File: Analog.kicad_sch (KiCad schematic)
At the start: 42 parts, among them IC1 AMC1350DWVR, IC2 AMC1350DWVR, IC3 ZXRE160AET5TA, U2 TLV9001IDBVR, U3 TLV9001IDBVR

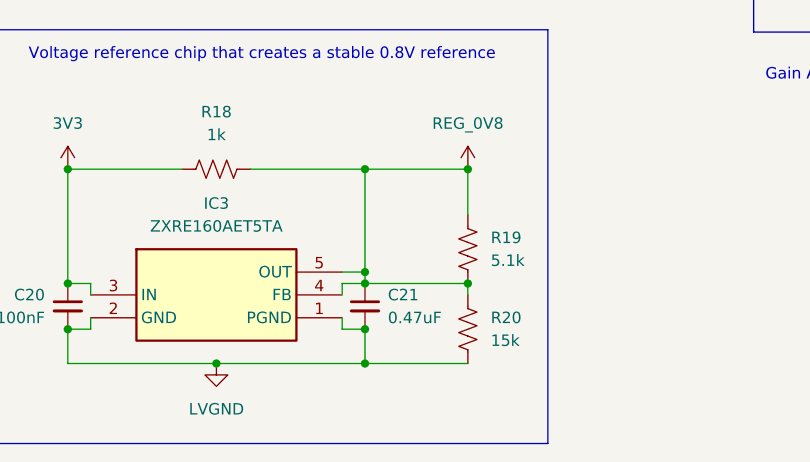
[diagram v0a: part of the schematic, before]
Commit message: Fixed 0.8V reference circuit short on accidental node for divider side
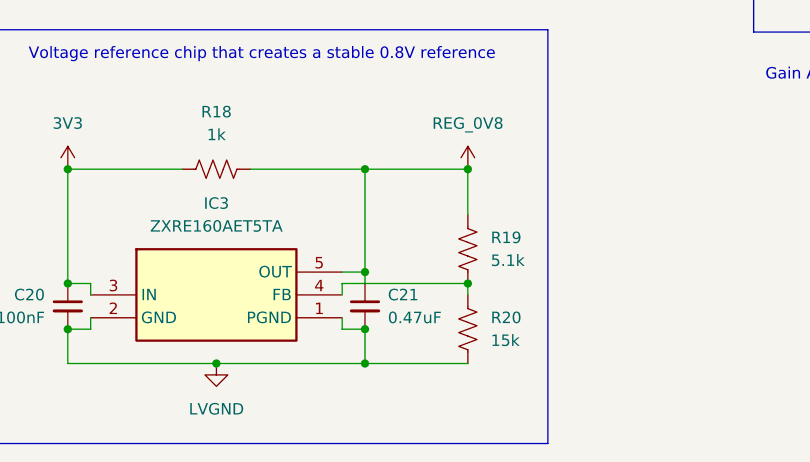
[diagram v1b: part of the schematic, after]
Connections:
- net REG_0V8: no longer IC3.4 (FB), R19.1, R20.1
- new net: IC3.4 (FB), R19.1, R20.1
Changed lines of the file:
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@@
-	)
-	(junction
-		(at 144.78 144.78)
-		(diameter 0)
-		(color 0 0 0 0)
 	)
 	(junction
@@
 	)
 	(junction
+		(at 66.04 53.34)
+		(diameter 0)
+		(color 0 0 0 0)
+	)
+	(junction
+		(at 218.44 54.61)
+		(diameter 0)
+		(color 0 0 0 0)
+	)
+	(junction
+		(at 36.83 53.34)
+		(diameter 0)
+		(color 0 0 0 0)
+	)
+	(junction
+		(at 229.87 67.31)
+		(diameter 0)
+		(color 0 0 0 0)
+	)
+	(junction
+		(at 157.48 59.69)
+		(diameter 0)
+		(color 0 0 0 0)
+	)
+	(junction
+		(at 128.27 153.67)
+		(diameter 0)
+		(color 0 0 0 0)
+	)
+	(junction
+		(at 116.84 46.99)
+		(diameter 0)
+		(color 0 0 0 0)
+	)
+	(junction
+		(at 77.47 53.34)
+		(diameter 0)
+		(color 0 0 0 0)
+	)
+	(junction
+		(at 144.78 132.08)
+		(diameter 0)
+		(color 0 0 0 0)
+	)
+	(junction
+		(at 156.21 132.08)
+		(diameter 0)
+		(color 0 0 0 0)
+	)
+	(junction
+		(at 116.84 82.55)
+		(diameter 0)
+		(color 0 0 0 0)
+	)
+	(junction
+		(at 124.46 54.61)
+		(diameter 0)
+		(color 0 0 0 0)
+	)
+	(junction
+		(at 157.48 90.17)
+		(diameter 0)
+		(color 0 0 0 0)
+	)
+	(junction
+		(at 116.84 87.63)
+		(diameter 0)
+		(color 0 0 0 0)
+	)
+	(junction
 		(at 156.21 144.78)
 		(diameter 0)
@@
 	)
 	(junction
-		(at 66.04 53.34)
-		(diameter 0)
-		(color 0 0 0 0)
-	)
-	(junction
-		(at 218.44 54.61)
-		(diameter 0)
-		(color 0 0 0 0)
-	)
-	(junction
-		(at 36.83 53.34)
-		(diameter 0)
-		(color 0 0 0 0)
-	)
-	(junction
-		(at 229.87 67.31)
-		(diameter 0)
-		(color 0 0 0 0)
-	)
-	(junction
-		(at 157.48 59.69)
-		(diameter 0)
-		(color 0 0 0 0)
-	)
-	(junction
-		(at 128.27 153.67)
-		(diameter 0)
-		(color 0 0 0 0)
-	)
-	(junction
-		(at 116.84 46.99)
-		(diameter 0)
-		(color 0 0 0 0)
-	)
-	(junction
-		(at 77.47 53.34)
-		(diameter 0)
-		(color 0 0 0 0)
-	)
-	(junction
-		(at 144.78 132.08)
-		(diameter 0)
-		(color 0 0 0 0)
-	)
-	(junction
-		(at 156.21 132.08)
-		(diameter 0)
-		(color 0 0 0 0)
-	)
-	(junction
-		(at 116.84 82.55)
-		(diameter 0)
-		(color 0 0 0 0)
-	)
-	(junction
-		(at 124.46 54.61)
-		(diameter 0)
-		(color 0 0 0 0)
-	)
-	(junction
-		(at 157.48 90.17)
-		(diameter 0)
-		(color 0 0 0 0)
-	)
-	(junction
-		(at 116.84 87.63)
-		(diameter 0)
-		(color 0 0 0 0)
-	)
-	(junction
 		(at 111.76 144.78)
 		(diameter 0)
@@
 	(wire
 		(pts
-			(xy 142.24 144.78) (xy 144.78 144.78)
-		)
-		(stroke
-			(width 0)
-			(type default)
-		)
-	)
-	(wire
-		(pts
 			(xy 124.46 81.28) (xy 127 81.28)
 		)
@@
 	(wire
 		(pts
-			(xy 144.78 144.78) (xy 156.21 144.78)
-		)
-		(stroke
-			(width 0)
-			(type default)
-		)
-	)
-	(wire
-		(pts
 			(xy 144.78 132.08) (xy 156.21 132.08)
 		)
@@
 		)
 		(stroke
+			(width 0)
+			(type default)
+		)
+	)
+	(wire
+		(pts
+			(xy 142.24 144.78) (xy 156.21 144.78)
+		)
+		(stroke

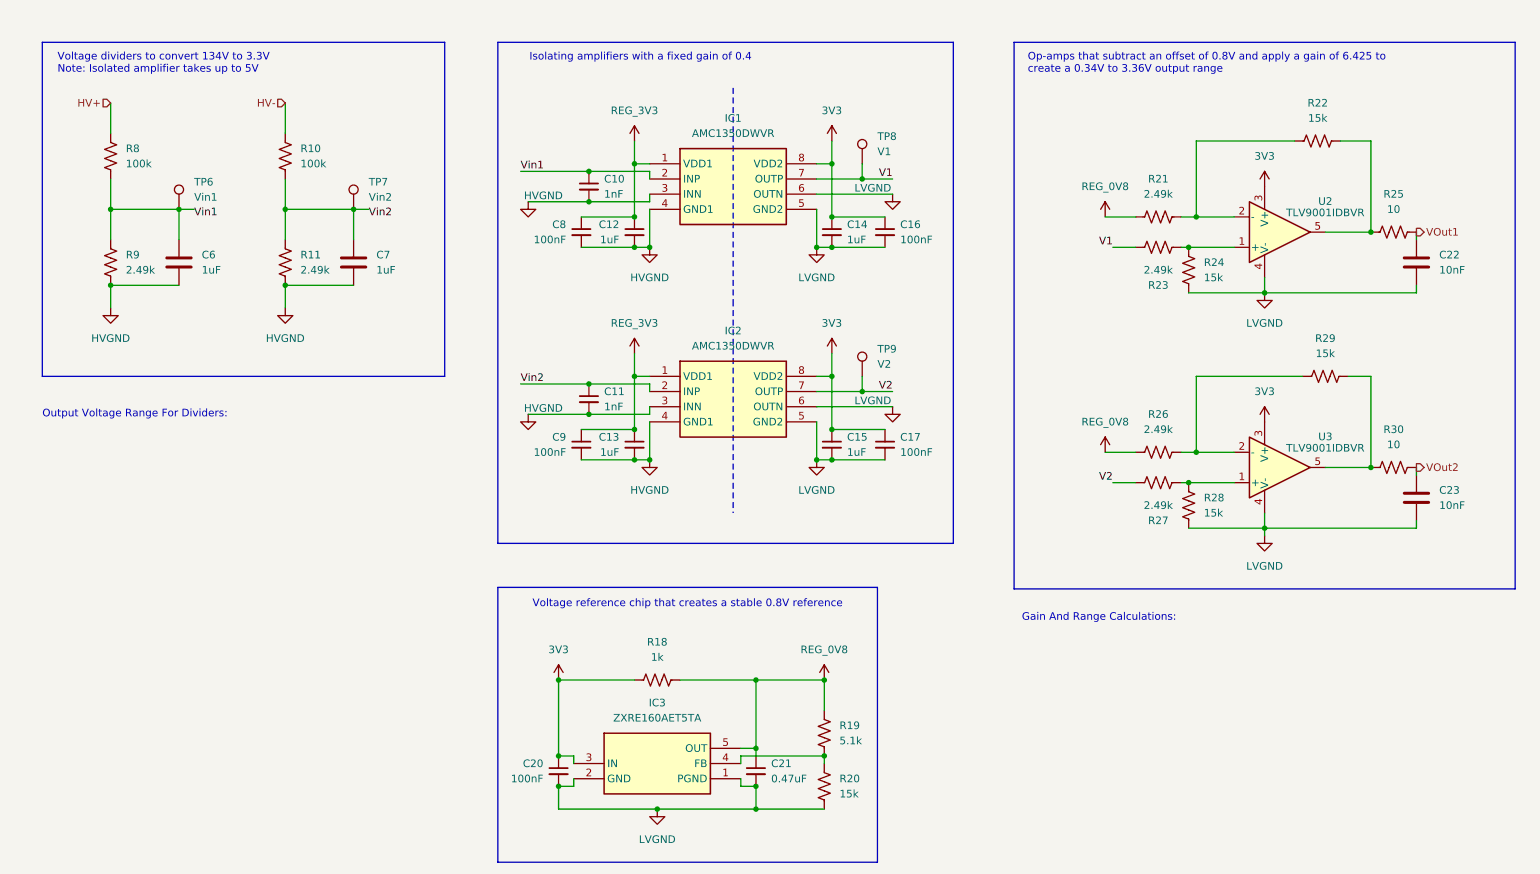
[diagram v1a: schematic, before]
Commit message: Removed the 0.8V Reference circuit, changed the opamp, and changed the testpoints to make testing easier. Not sure how the connector is meant to be set up though
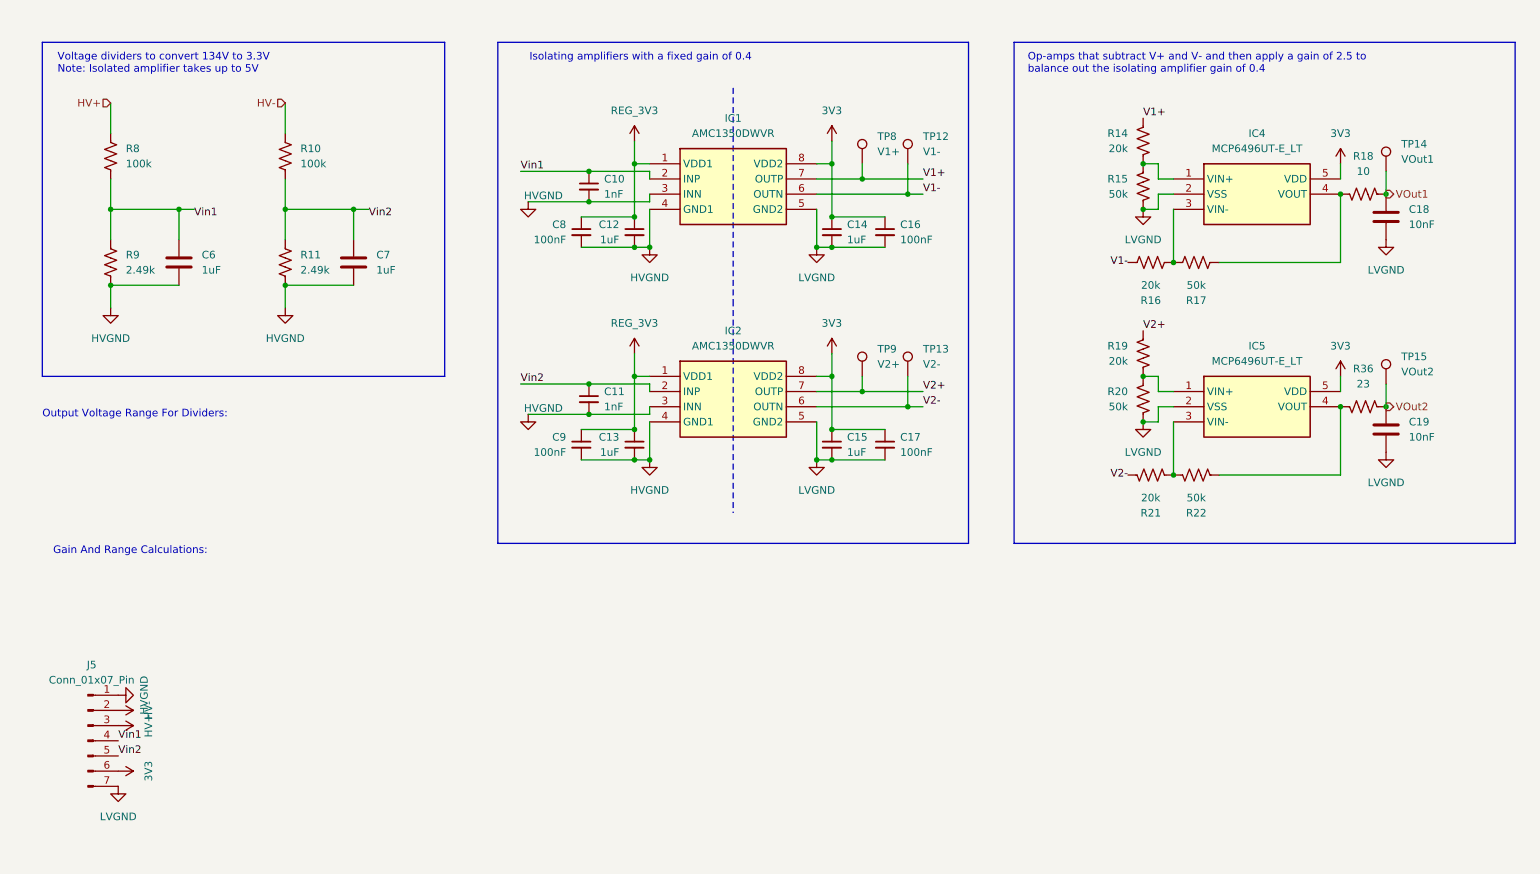
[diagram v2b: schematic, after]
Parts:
- removed C20: 100nF, Capacitor_SMD:C_0603_1608Metric_Pad1.08x0.95mm_HandSolder, symbol Device:C_Small
- removed C21: 0.47uF, Capacitor_SMD:C_0603_1608Metric_Pad1.08x0.95mm_HandSolder, symbol Device:C_Small
- removed C22, C23: 10nF, Capacitor_SMD:C_0603_1608Metric_Pad1.08x0.95mm_HandSolder, symbol Device:C
- removed IC3: ZXRE160AET5TA, ActivePrecharge-RevB:SOT95P280X100-5N, symbol VREF:ZXRE160AET5TA
- removed R23, R26, R27: 2.49k, Resistor_SMD:R_0603_1608Metric_Pad0.98x0.95mm_HandSolder, symbol Device:R_US
- removed R24, R28, R29: 15k, Resistor_SMD:R_0603_1608Metric_Pad0.98x0.95mm_HandSolder, symbol Device:R_US
- removed R25, R30: 10, Resistor_SMD:R_0603_1608Metric_Pad0.98x0.95mm_HandSolder, symbol Device:R_US
- removed TP6: Vin1, TestPoint:TestPoint_THTPad_D1.0mm_Drill0.5mm, symbol Connector:TestPoint
- removed TP7: Vin2, TestPoint:TestPoint_THTPad_D1.0mm_Drill0.5mm, symbol Connector:TestPoint
- removed U2, U3: TLV9001IDBVR, ActivePrecharge-RevB:DBV0005A_N, symbol Simulation_SPICE:OPAMP
- added C18, C19: 10nF, Capacitor_SMD:C_0603_1608Metric_Pad1.08x0.95mm_HandSolder, symbol Device:C
- added IC4, IC5: MCP6496UT-E_LT, ActivePrecharge-RevB:SOT65P210X110-5N, symbol DIFF-AMP:MCP6496UT-E_LT
- added J5: Conn_01x07_Pin, Connector_PinHeader_2.54mm:PinHeader_1x07_P2.54mm_Vertical, symbol Connector:Conn_01x07_Pin
- added R14, R16: 20k, Resistor_SMD:R_0603_1608Metric_Pad0.98x0.95mm_HandSolder, symbol Device:R_US
- added R15, R17: 50k, Resistor_SMD:R_0603_1608Metric_Pad0.98x0.95mm_HandSolder, symbol Device:R_US
- added R36: 23, Resistor_SMD:R_0603_1608Metric_Pad0.98x0.95mm_HandSolder, symbol Device:R_US
- added TP12: V1-, TestPoint:TestPoint_Pad_2.0x2.0mm, symbol Connector:TestPoint
- added TP13: V2-, TestPoint:TestPoint_Pad_2.0x2.0mm, symbol Connector:TestPoint
- added TP14: VOut1, TestPoint:TestPoint_Pad_2.0x2.0mm, symbol Connector:TestPoint
- added TP15: VOut2, TestPoint:TestPoint_Pad_2.0x2.0mm, symbol Connector:TestPoint
- R18: value 1k -> 10; P/N CRCW06031K00FKEI -> CRCW06032K49FKEAC
- R19: value 5.1k -> 20k; P/N CRCW06035K10FKEC -> CRCW06032K49FKEAC
- R20, R22: value 15k -> 50k; P/N CRCW060315K0FKEA -> CRCW06032K49FKEAC
- R21: value 2.49k -> 20k
- TP8: value V1 -> V1+; footprint TestPoint:TestPoint_THTPad_D1.0mm_Drill0.5mm -> TestPoint:TestPoint_Pad_2.0x2.0mm
- TP9: value V2 -> V2+; footprint TestPoint:TestPoint_THTPad_D1.0mm_Drill0.5mm -> TestPoint:TestPoint_Pad_2.0x2.0mm
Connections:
- net 3V3: now also IC4.5 (VDD), IC5.5 (VDD), J5.6 (Pin_6); no longer R18.1
- net HV+: now also J5.3 (Pin_3)
- net HV-: now also J5.2 (Pin_2)
- net HVGND: now also J5.1 (Pin_1)
- net LVGND: now also R20.1, C18.2, C19.2, IC4.2 (VSS), IC5.2 (VSS), J5.7 (Pin_7), R15.1; no longer IC1.6 (OUTN), IC2.6 (OUTN), R20.2
- net VOut1: now also R18.1, C18.1, TP14.1
- net VOut2: now also C19.1, R36.1, TP15.1
- net Vin1: now also J5.4 (Pin_4)
- net Vin2: now also J5.5 (Pin_5)
- net at R22.1: now also IC5.4 (VOUT), R36.2
- net at R22.2: now also R21.1, IC5.3 (VIN-); no longer R21.2
- net at R19.1: now also R20.2, IC5.1 (VIN+); no longer R20.1
- removed net REG_0V8: R18.2, R19.2, R21.1
- net V1 renamed V1+
- net V1+: now also R14.2
- net V2 renamed V2+
- net V2+: now also R19.2
- new net: IC4.1 (VIN+), R14.1, R15.2
- new net: IC4.4 (VOUT), R17.1, R18.2
- new net: IC4.3 (VIN-), R16.1, R17.2
- new net V1-: IC1.6 (OUTN), R16.2, TP12.1
- new net V2-: IC2.6 (OUTN), R21.2, TP13.1
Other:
- note added: "Op-amps that subtract V+ and V- and then apply a gain of 2.5 to balance out the isolating amplifier gain of 0.4"
- note removed: "Op-amps that subtract an offset of 0.8V and apply a gain of 6.425 to create a 0.34V to 3.36V output range"
- note removed: "Voltage reference chip that creates a stable 0.8V reference"

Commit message: Changed opamp to the TLV9002QDRQ1, separated the pin test points, changed 24V LED resitors to 10k (I don't remember what resistance you guys said), made 2 hierarchical sheets that are linked copies, grouped the calculation for easy reading, and I forgot what other math you wanted me to add that I didn't show.
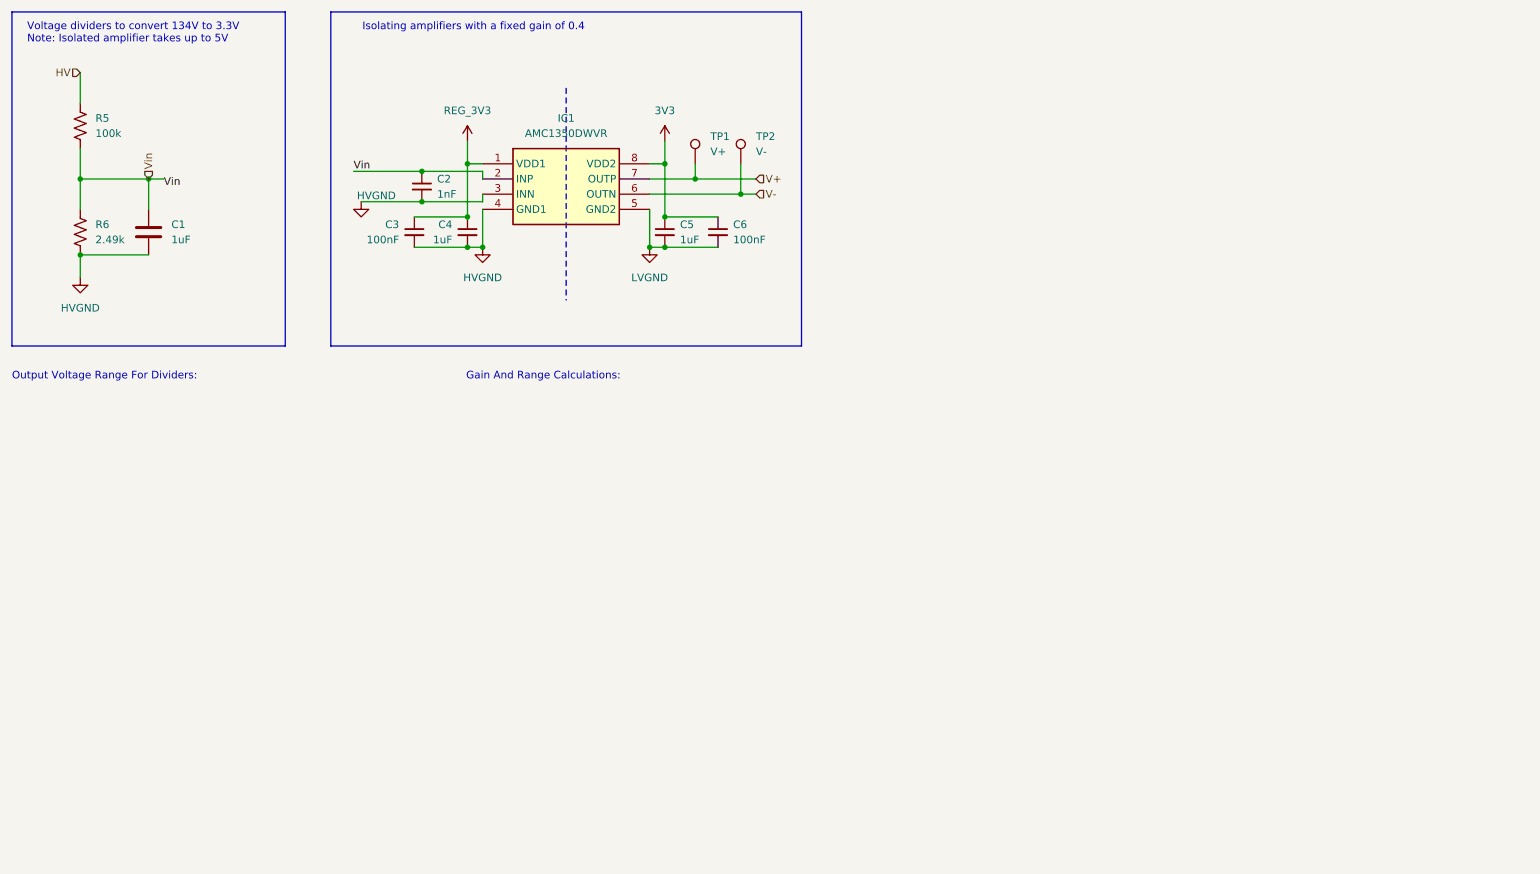
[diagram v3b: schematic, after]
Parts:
- removed C11: 1nF, Capacitor_SMD:C_0603_1608Metric_Pad1.08x0.95mm_HandSolder, symbol Device:C_Small
- removed C13, C15: 1uF, Capacitor_SMD:C_0603_1608Metric_Pad1.08x0.95mm_HandSolder, symbol Device:C_Small
- removed C17, C9: 100nF, Capacitor_SMD:C_0603_1608Metric_Pad1.08x0.95mm_HandSolder, symbol Device:C_Small
- removed C18, C19: 10nF, Capacitor_SMD:C_0603_1608Metric_Pad1.08x0.95mm_HandSolder, symbol Device:C
- removed C7: 1uF, Capacitor_SMD:C_0603_1608Metric_Pad1.08x0.95mm_HandSolder, symbol Device:C
- removed IC2: AMC1350DWVR, ActivePrecharge-RevB:SOIC127P1150X280-8N, symbol AMC1350:AMC1350DWVR
- removed IC4, IC5: MCP6496UT-E_LT, ActivePrecharge-RevB:SOT65P210X110-5N, symbol DIFF-AMP:MCP6496UT-E_LT
- removed J5: Conn_01x07_Pin, Connector_PinHeader_2.54mm:PinHeader_1x07_P2.54mm_Vertical, symbol Connector:Conn_01x07_Pin
- removed R10: 100k, Resistor_SMD:R_0603_1608Metric_Pad0.98x0.95mm_HandSolder, symbol Device:R_US
- removed R11: 2.49k, Resistor_SMD:R_0603_1608Metric_Pad0.98x0.95mm_HandSolder, symbol Device:R_US
- removed R14, R16, R19, R21: 20k, Resistor_SMD:R_0603_1608Metric_Pad0.98x0.95mm_HandSolder, symbol Device:R_US
- removed R15, R17, R20, R22: 50k, Resistor_SMD:R_0603_1608Metric_Pad0.98x0.95mm_HandSolder, symbol Device:R_US
- removed R18: 10, Resistor_SMD:R_0603_1608Metric_Pad0.98x0.95mm_HandSolder, symbol Device:R_US
- removed R36: 23, Resistor_SMD:R_0603_1608Metric_Pad0.98x0.95mm_HandSolder, symbol Device:R_US
- removed TP13: V2-, TestPoint:TestPoint_Pad_2.0x2.0mm, symbol Connector:TestPoint
- removed TP14: VOut1, TestPoint:TestPoint_Pad_2.0x2.0mm, symbol Connector:TestPoint
- removed TP15: VOut2, TestPoint:TestPoint_Pad_2.0x2.0mm, symbol Connector:TestPoint
- removed TP9: V2+, TestPoint:TestPoint_Pad_2.0x2.0mm, symbol Connector:TestPoint
- TP1: renamed from TP8; value V1+ -> V+
- TP2: renamed from TP12; value V1- -> V-
- renumbered C6 to C1, C10 to C2, C8 to C3, C12 to C4, C14 to C5, C16 to C6, R8 to R5, R9 to R6
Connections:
- net HV+ renamed HV
- net V1+ renamed V+
- net V1- renamed V-
- net Vin1 renamed Vin
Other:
- note removed: "Op-amps that subtract V+ and V- and then apply a gain of 2.5 to balance out the isolating amplifier gain of 0.4"
- moved on the sheet: C1, C2, C3, C4, C5, C6, IC1, R5, R6, TP1, TP2
